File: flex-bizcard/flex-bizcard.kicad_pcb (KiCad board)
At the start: 2 copper layers, 35.9 x 20.8 mm, 2 parts

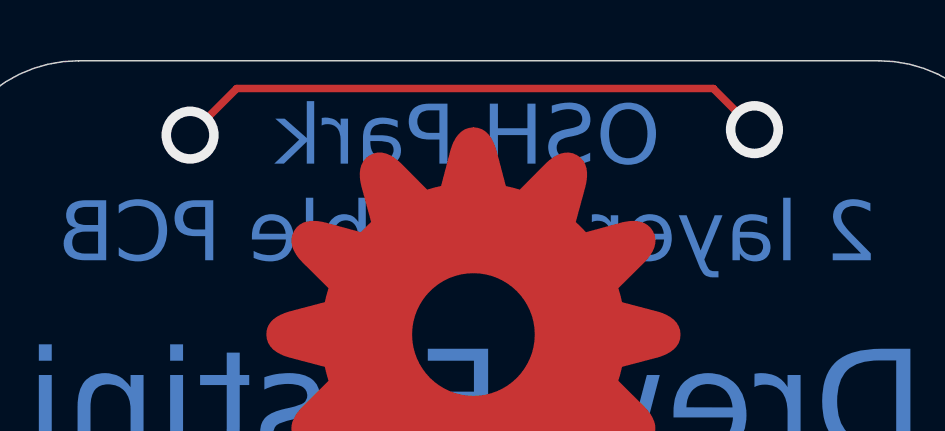
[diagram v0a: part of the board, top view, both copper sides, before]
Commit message: create schematic and relayout flex batt tester
the teardrop plugin needs a schematic to work properly:
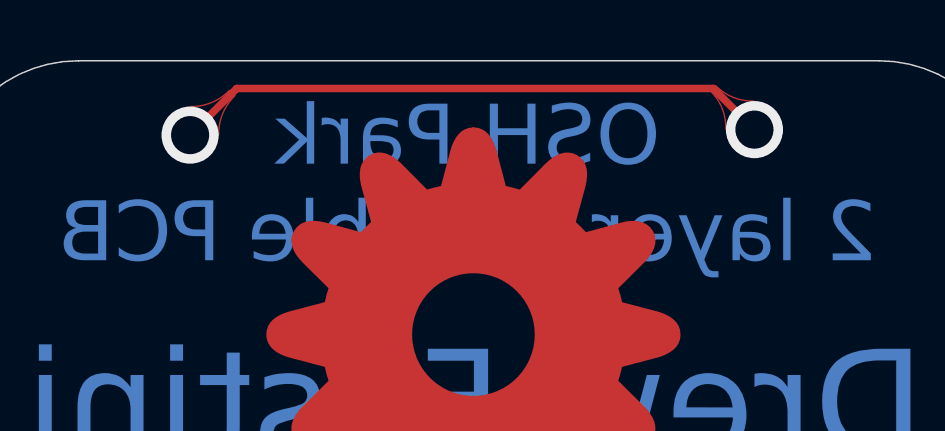
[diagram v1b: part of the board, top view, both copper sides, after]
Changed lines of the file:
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@@
   (segment (start 135.03148 64.20104) (end 136.58596 62.64656) (width 0.25) (layer F.Cu) (net 0))
   (segment (start 136.58596 62.64656) (end 152.47112 62.64656) (width 0.25) (layer F.Cu) (net 0))
+  (zone (net 0) (net_name "") (layer F.Cu) (hatch edge 0.508)
+    (priority 16962)
+    (connect_pads yes (clearance 0.2))
+    (min_thickness 0.0254)
+    (fill yes (arc_segments 32) (thermal_gap 0.508) (thermal_bridge_width 0.508))
+    (polygon
+      (pts
+        (xy 152.382732 62.734949) (xy 152.480529 62.840407) (xy 152.567872 62.950735) (xy 152.644761 63.065931) (xy 152.711196 63.185997)
+        (xy 152.767177 63.310931) (xy 152.812704 63.440734) (xy 152.847776 63.575406) (xy 152.872394 63.714947) (xy 152.886558 63.859356)
+        (xy 152.890268 64.008635) (xy 154.179479 64.354919) (xy 153.833195 63.065708) (xy 153.683916 63.061998) (xy 153.539507 63.047834)
+        (xy 153.399966 63.023216) (xy 153.265294 62.988144) (xy 153.135491 62.942617) (xy 153.010557 62.886636) (xy 152.890491 62.820201)
+        (xy 152.775295 62.743312) (xy 152.664967 62.655969) (xy 152.559509 62.558172)
+      )
+    )
+  )
+  (zone (net 0) (net_name "") (layer F.Cu) (hatch edge 0.508)
+    (priority 16962)
+    (connect_pads yes (clearance 0.2))
+    (min_thickness 0.0254)
+    (fill yes (arc_segments 32) (thermal_gap 0.508) (thermal_bridge_width 0.508))
+    (polygon
+      (pts
+        (xy 136.355714 62.700029) (xy 136.24246 62.80562) (xy 136.125159 62.899938) (xy 136.003809 62.98298) (xy 135.87841 63.054748)
+        (xy 135.748964 63.115241) (xy 135.615469 63.16446) (xy 135.477925 63.202404) (xy 135.336333 63.229073) (xy 135.190693 63.244468)
+        (xy 135.041005 63.248588) (xy 134.694721 64.537799) (xy 135.983932 64.191515) (xy 135.988051 64.041826) (xy 136.003446 63.896186)
+        (xy 136.030115 63.754594) (xy 136.068059 63.61705) (xy 136.117278 63.483555) (xy 136.177771 63.354109) (xy 136.249539 63.22871)
+        (xy 136.332581 63.10736) (xy 136.426899 62.990059) (xy 136.532491 62.876806)
+      )
+    )
+  )
 )
